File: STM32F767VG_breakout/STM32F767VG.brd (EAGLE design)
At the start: 100 x 80 mm, 44 parts, among them IC1 STM32F767VGT6, IC3 LD117AS33TR, X4 8MHz, X5 32.768kHz, X6 MSTBA2

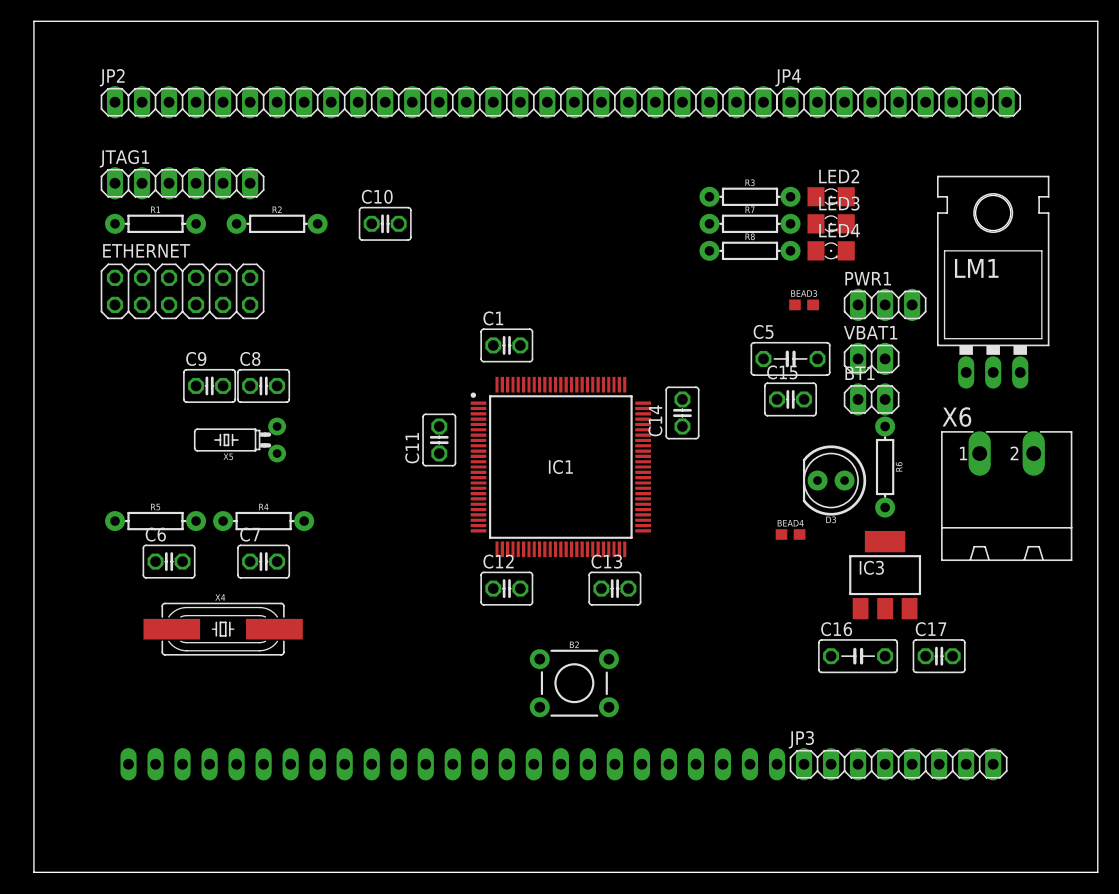
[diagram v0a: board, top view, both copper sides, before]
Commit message: Organized components in the .brd file
Still have to route it
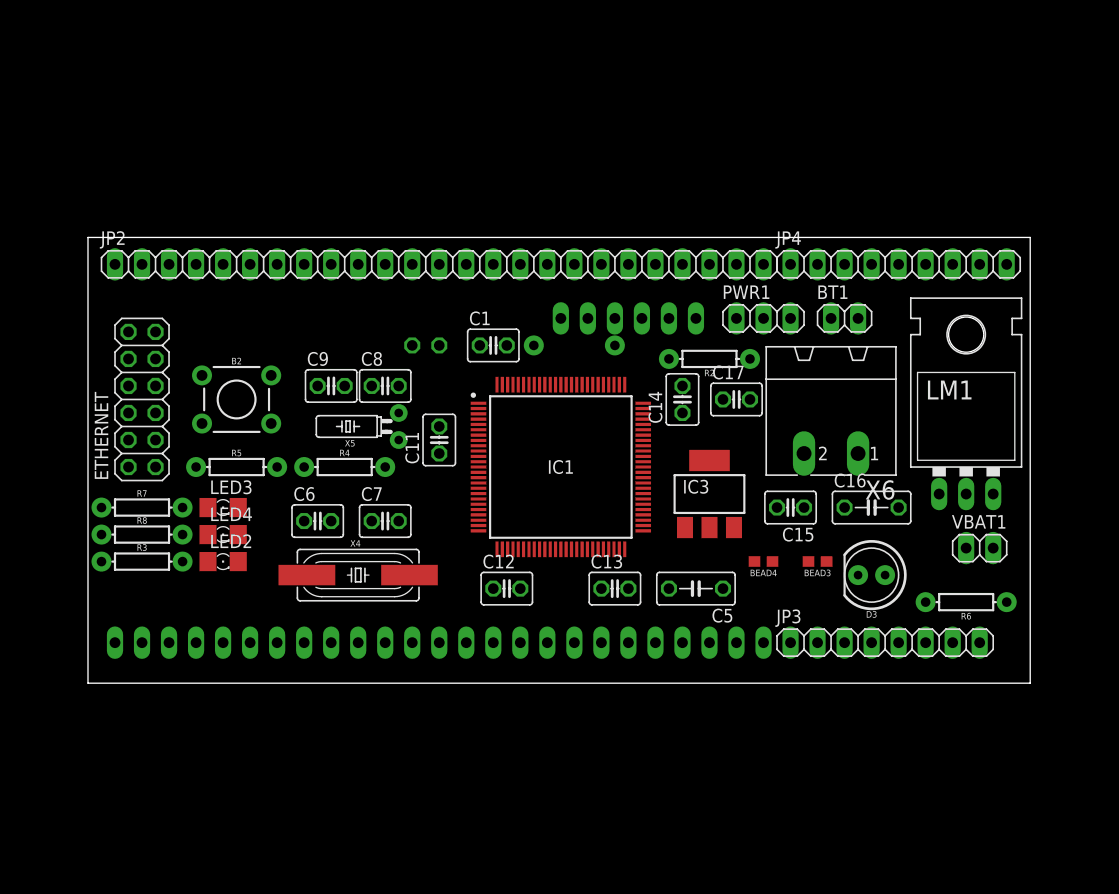
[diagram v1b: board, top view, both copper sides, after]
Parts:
- moved LED2 66.6 mm to (17.8, 29.2)
- moved R3 66.6 mm to (10.2, 29.2)
- moved LED3 63.1 mm to (17.8, 34.3)
- moved LED4 63.1 mm to (17.8, 31.8)
- moved R7 63.1 mm to (10.2, 34.3)
- moved R8 63.1 mm to (10.2, 31.8)
- moved JTAG1 43.8 mm to (55.9, 52.1), flipped to the bottom
- moved R2 42.6 mm to (63.5, 48.3), turned to 180 degrees
- moved B2 41.5 mm to (19.1, 44.5)
- moved R1 41.0 mm to (50.8, 49.5), flipped to the bottom
- moved C17 30.7 mm to (66.0, 44.5)
- moved BEAD3 24.2 mm to (73.7, 29.2), turned to 180 degrees
- moved C5 23.3 mm to (62.2, 26.7), turned to 180 degrees
- moved VBAT1 20.5 mm to (88.9, 30.5)
- moved X6 19.4 mm to (74.9, 44.5), turned to 180 degrees
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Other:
- board size 100 x 80 mm -> 88.6 x 41.9 mm

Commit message: Mar 26 Feedback incorporated
Verification for correct 100nF cap package required. As per crystal datasheet, traces from crystal to microcontroller were minimized.
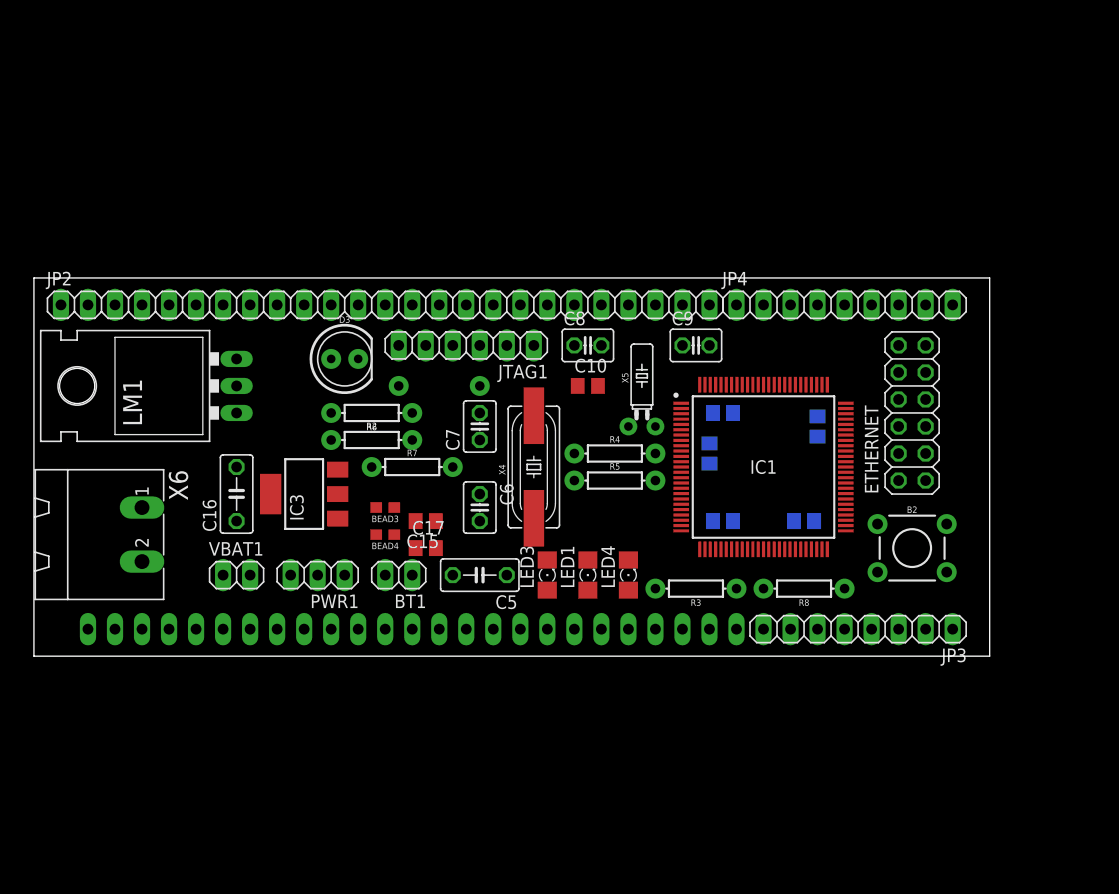
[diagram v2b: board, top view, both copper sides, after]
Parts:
- removed LED2: (no value), eagle-ltspice:LED_1206
- added LED1: (no value), eagle-ltspice:LED_1206
- C1, C10, C11, C12, C13, C14, C15, C17: device ee2parts:C025-030X050 -> eagle-ltspice:C0805
- moved LM1 72.7 mm to (15.2, 45.7), turned to 90 degrees
- moved ETHERNET 72.4 mm to (82.5, 43.2)
- moved X6 71.0 mm to (5.08, 31.8), turned to 270 degrees
- moved VBAT1 69.9 mm to (19.1, 27.9)
- moved B2 65.0 mm to (82.5, 30.5)
- moved R8 62.4 mm to (72.4, 26.7), turned to 180 degrees
- moved C16 59.7 mm to (19.1, 35.6), turned to 90 degrees
- moved R6 58.6 mm to (31.8, 43.2)
- moved D3 53.5 mm to (29.2, 48.3), turned to 0 degrees
- moved R3 52.1 mm to (62.2, 26.7), turned to 180 degrees
- moved BT1 48.4 mm to (34.3, 27.9), turned to 180 degrees
- moved PWR1 48.4 mm to (26.7, 27.9), turned to 180 degrees
- moved BEAD3 41.0 mm to (33.0, 34.3)
- moved LED4 38.3 mm to (55.9, 27.9), turned to 90 degrees
- moved IC3 38.1 mm to (25.4, 35.6), turned to 90 degrees
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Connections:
- net GND: now also LED1.C; no longer LED2.C
- net N$17: now also LED1.A; no longer LED2.A
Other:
- board size 88.6 x 41.9 mm -> 89.8 x 35.5 mm

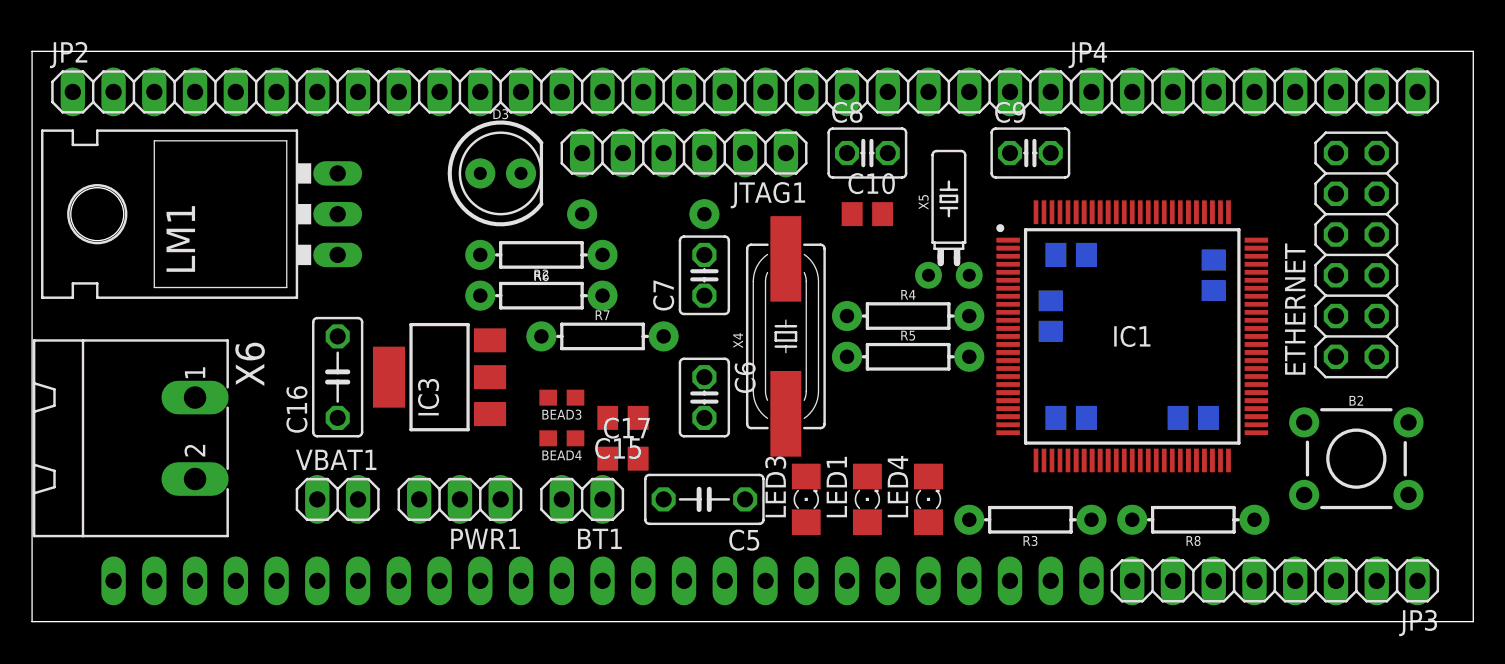
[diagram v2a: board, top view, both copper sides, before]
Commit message: Apr 2 Feedback incorporated
Please check if the surface mount of resistors, caps, and LEDs are ok. Also, I noticed there's a lot of free space.
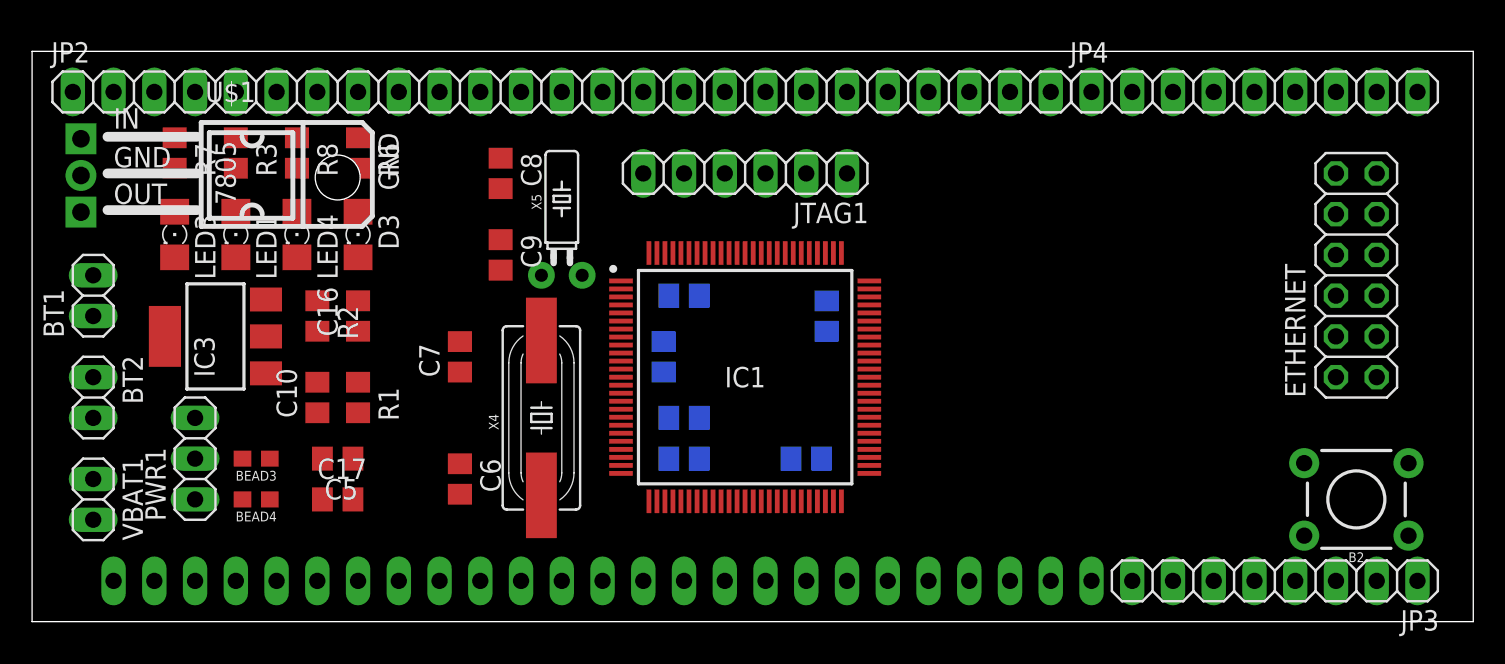
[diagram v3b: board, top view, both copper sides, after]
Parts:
- removed LM1: (no value), SparkFun-IC-Power:TO-220-ALT
- removed R4, R5: 1k, SparkFun-Resistors:AXIAL-0.3
- removed X6: MSTBA2, con-phoenix-508:MSTBA2
- added BT2: (no value), pinhead:1X02
- added U$1: -L7805, tango:L7805
- C16, C5: device ee2parts:C050-030-075 -> eagle-ltspice:C0805
- C6, C7, C8, C9: device ee2parts:C025-030X050 -> eagle-ltspice:C0805
- D3: device SparkFun-LED:LED_5MM -> eagle-ltspice:LED_1206
- R1, R2, R3, R6, R7, R8: device SparkFun-Resistors:AXIAL-0.3 -> eagle-ltspice:R0805
- moved R8 60.4 mm to (16.5, 49.5), turned to 270 degrees
- moved R3 54.6 mm to (12.7, 49.5), turned to 270 degrees
- moved LED1 42.7 mm to (12.7, 44.5), turned to 270 degrees
- moved LED4 42.7 mm to (16.5, 44.5), turned to 270 degrees
- moved LED3 42.7 mm to (8.89, 44.5), turned to 270 degrees
- moved C10 36.1 mm to (17.8, 34.3), turned to 90 degrees
- moved C9 33.6 mm to (29.2, 43.2), turned to 270 degrees
- moved BT1 33.0 mm to (3.81, 40.6), turned to 90 degrees
- moved R7 29.0 mm to (8.89, 49.5), turned to 270 degrees
- moved C13 24.3 mm to (48.3, 30.5)
- moved C11 24.3 mm to (39.4, 36.8)
- moved C12 24.3 mm to (40.6, 30.5)
- moved C1 24.3 mm to (40.6, 40.6)
- moved C14 24.3 mm to (49.5, 39.4)
- moved IC1 24.3 mm to (44.5, 35.6)
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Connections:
- removed net N$16: IC1.12, R4.P$2
- removed net N$19: IC1.13, R5.P$2
- net 12V: now also BT2.1, U$1.IN; no longer LM1.IN, X6.1
- net 5V: now also U$1.OUT; no longer LM1.OUT
- net BOOT0: now also R2.1; no longer R2.P$1
- net GND: now also D3.C, R2.2, U$1.GND; no longer D3.K, LM1.GND, R2.P$2
- net MGND: now also BT2.2; no longer X6.2
- net N$17: now also R3.2; no longer R3.P$2
- net N$21: now also IC1.13; no longer R5.P$1
- net N$22: now also IC1.12; no longer R4.P$1
- net N$23: now also R6.2; no longer R6.P$2
- net N$26: now also R7.2; no longer R7.P$2
- net N$27: now also R8.2; no longer R8.P$2
- net NRST: now also R1.2; no longer R1.P$2
- net PD14: now also R8.1; no longer R8.P$1
- net PD15: now also R3.1; no longer R3.P$1
- net PD7: now also R7.1; no longer R7.P$1
- net VDD: now also R1.1, R6.1; no longer R1.P$1, R6.P$1

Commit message: Incorporated April 6 Comments
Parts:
- removed U$1: -L7805, tango:L7805
- added IC2: L7805CV, L7805CV:TO270P460X1020X2008-3P
- moved BEAD3 24.7 mm to (38.1, 25.4)
- moved BT1 16.3 mm to (14.0, 27.9)
- moved BEAD4 5.08 mm to (14.0, 33.0)
- moved PWR1 1.80 mm to (8.89, 29.2)
- flipped C10 to the bottom
- flipped C16 to the bottom
- flipped C17 to the bottom
- flipped C5 to the bottom
- flipped C6 to the bottom
- flipped C7 to the bottom
- flipped C8 to the bottom
- flipped C9 to the bottom
- flipped R1 to the bottom
- flipped R2 to the bottom
- flipped R3 to the bottom
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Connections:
- net 12V: now also IC2.1; no longer U$1.IN
- net 5V: now also IC2.3; no longer U$1.OUT
- net GND: now also IC2.2; no longer U$1.GND

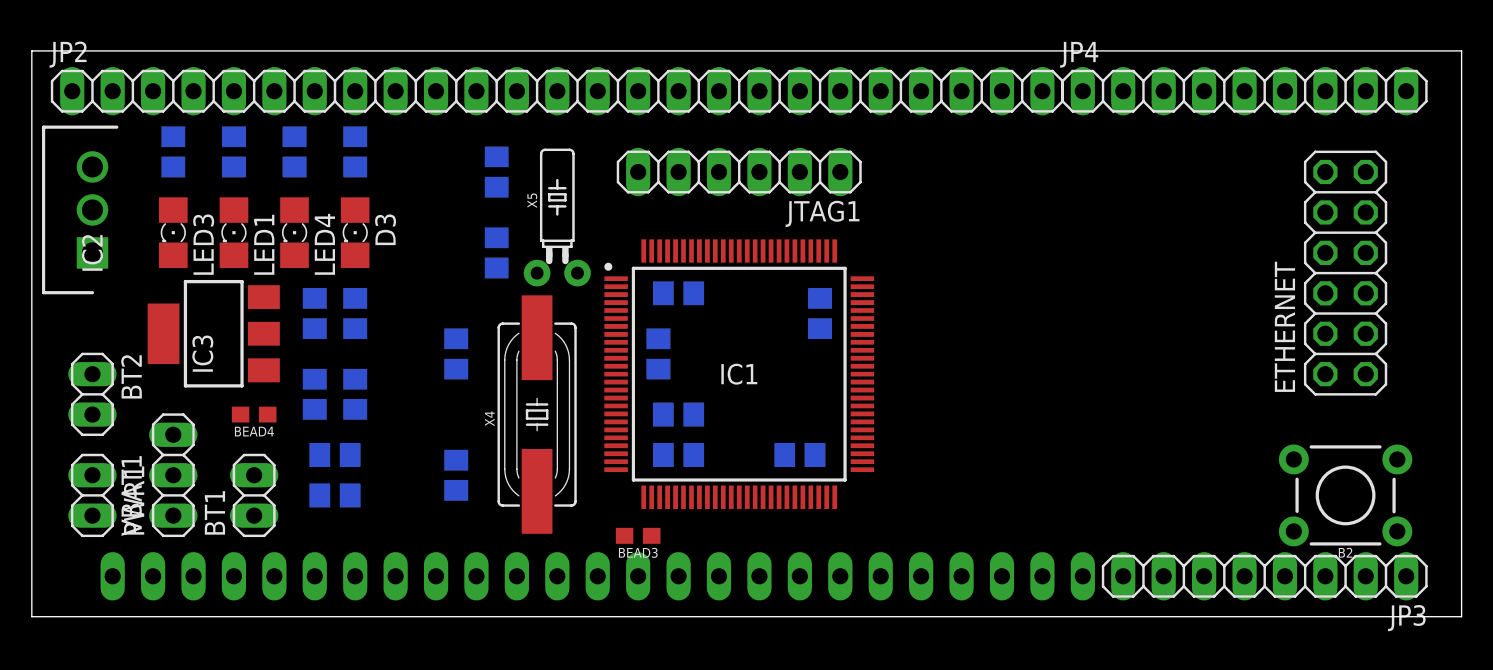
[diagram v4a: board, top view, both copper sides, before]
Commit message: Current routing progress
Routed most of top breakout pins
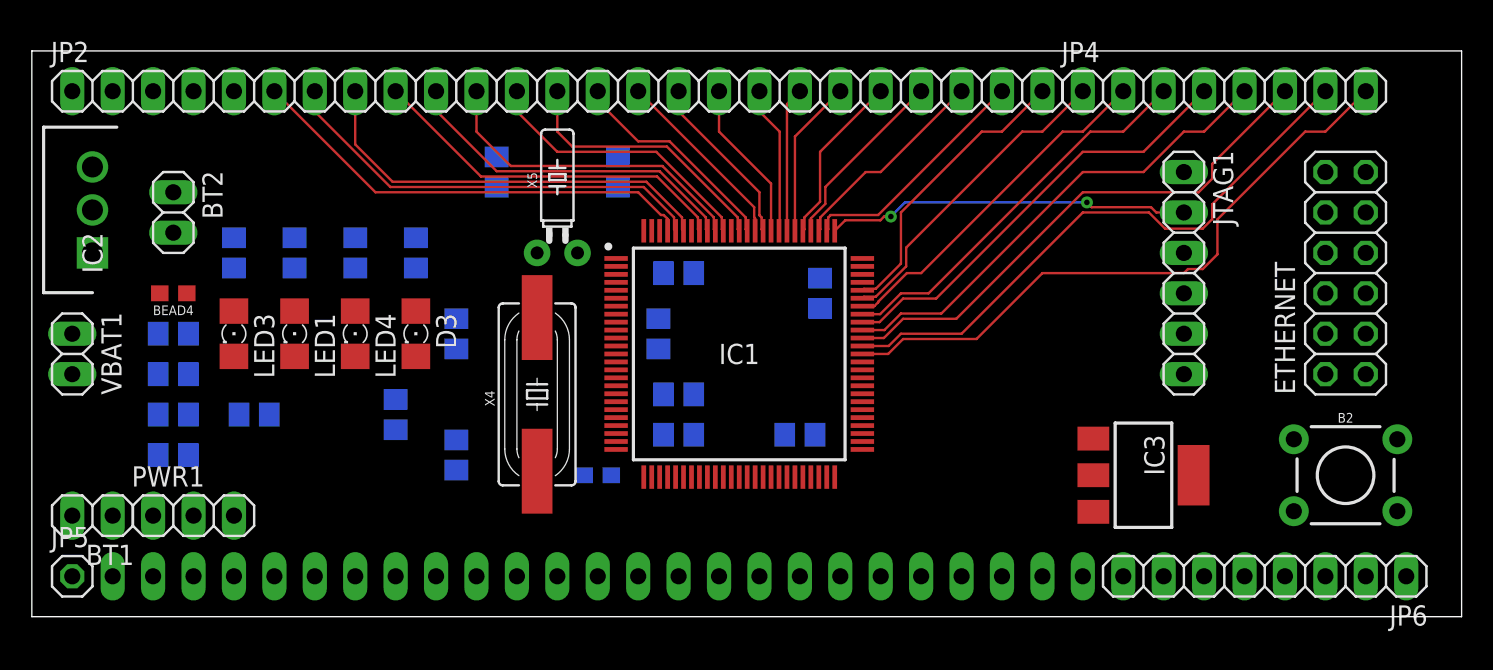
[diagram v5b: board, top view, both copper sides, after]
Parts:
- added JP5: (no value), pinhead:1X01
- JP4: device pinhead:1X09 -> pinhead:1X08
- moved IC3 59.1 mm to (69.8, 29.2), turned to 270 degrees
- moved JTAG1 28.7 mm to (72.4, 41.9), turned to 270 degrees
- moved C5 12.7 mm to (8.89, 38.1)
- moved BT2 12.5 mm to (8.89, 45.7)
- moved R2 10.9 mm to (8.89, 33.0), turned to 0 degrees
- moved C17 10.5 mm to (8.89, 30.5), turned to 180 degrees
- moved BT1 10.2 mm to (3.81, 26.7), turned to 180 degrees
- moved BEAD4 9.16 mm to (8.89, 40.6)
- moved C10 8.98 mm to (8.89, 35.6), turned to 0 degrees
- moved VBAT1 8.98 mm to (2.54, 36.8)
- moved C16 8.98 mm to (14.0, 33.0), turned to 0 degrees
- moved C8 7.62 mm to (36.8, 48.3)
- moved LED1 7.41 mm to (16.5, 38.1)
- moved R3 7.41 mm to (16.5, 43.2)
- moved D3 7.41 mm to (24.1, 38.1)
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- renumbered JP3 to JP6
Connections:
- net 12V: now also JP5.1; no longer JP4.9
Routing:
- net PC6: track 0.00 -> 39.8 mm
- net PC7: track 0.00 -> 37.1 mm
- net PC8: track 0.00 -> 33.5 mm
- net PC9: track 0.00 -> 30.2 mm
- net N$37: track 0.00 -> 28.8 mm
- net N$36: track 0.00 -> 27.5 mm
- net PA8: track 0.00 -> 27.5 mm
- net N$35: track 0.00 -> 26.7 mm
- net PA9: track 0.00 -> 24.7 mm
- net N$34: track 0.00 -> 23.2 mm
- net TCK: track 0.00 -> 22.9 mm, vias 0 -> 2
- net PA10: track 0.00 -> 22.0 mm
- net N$33: track 0.00 -> 21.8 mm
- net N$71: track 0.00 -> 20.6 mm
- net PA11: track 0.00 -> 19.9 mm
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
